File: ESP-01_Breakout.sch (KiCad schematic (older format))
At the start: 136 parts, among them J1 TBL003-254-02GR-2OR, SW1 SW_SPDT, U1 ESP-01v090, U2 R-78E5.0-0.5, U3 R-78E3.3-0.5

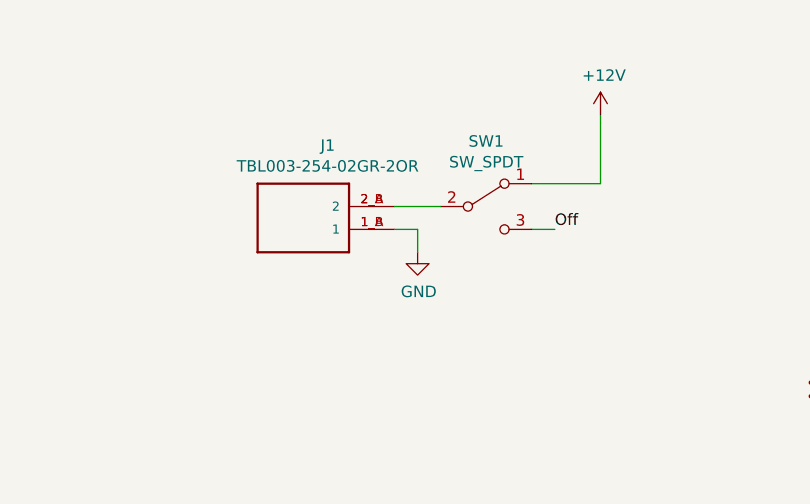
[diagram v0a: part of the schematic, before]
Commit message: Barrel Jack, Smaller Switch
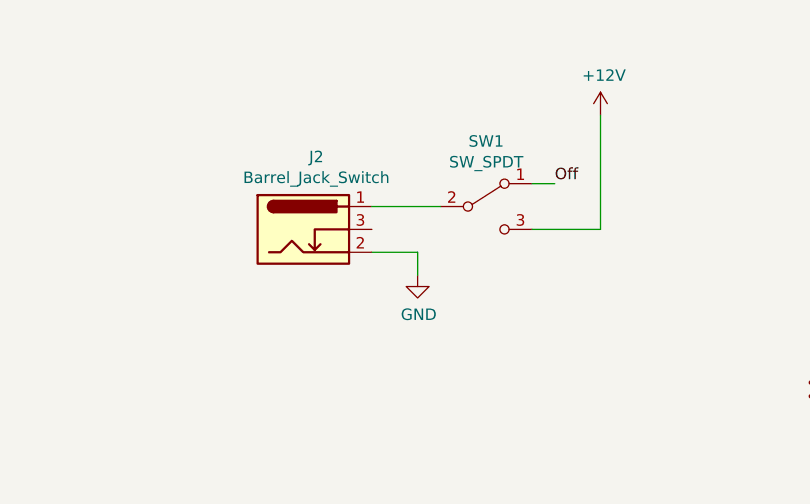
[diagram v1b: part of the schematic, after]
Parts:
- removed J1: TBL003-254-02GR-2OR, TBL003-254-02GR-2OR:CUI_TBL003-254-02GR-2OR, symbol TBL003-254-02GR-2OR:TBL003-254-02GR-2OR
- added J2: Barrel_Jack_Switch, ESP-01_Breakout:BarrelJack_Horizontal, symbol Connector:Barrel_Jack_Switch
- C1: footprint Capacitor_SMD:C_0805_2012Metric_Pad1.15x1.40mm_HandSolder -> Connector_BarrelJack:BarrelJack_Horizontal
- SW1: footprint ESP-01_Breakout:L102011ML04Q -> ESP-01_Breakout:SS312SAH4-R
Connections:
- net +12V: now also SW1.3 (C); no longer SW1.1 (A)
- net GND: now also J2.2
- net Off: now also SW1.1 (A); no longer SW1.3 (C)
- net at SW1.2 (B): now also J2.1
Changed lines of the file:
@@
 F 0 "C1" H 7315 2346 50  0000 L CNN
 F 1 "4.7uF" H 7315 2255 50  0000 L CNN
-F 2 "Capacitor_SMD:C_0805_2012Metric_Pad1.15x1.40mm_HandSolder" H 7238 2150 50  0001 C CNN
+F 2 "Connector_BarrelJack:BarrelJack_Horizontal" H 7238 2150 50  0001 C CNN
 F 3 "~" H 7200 2300 50  0001 C CNN
 F 4 "490-10751-1-ND" H 7200 2300 50  0001 C CNN "DigikeyPN"
@@
 	1100 3600 1200 3600
 $Comp
-L TBL003-254-02GR-2OR:TBL003-254-02GR-2OR J1
-U 1 1 5E644418
-P 4900 1500
-F 0 "J1" H 4793 1233 50  0000 C CNN
-F 1 "TBL003-254-02GR-2OR" H 4793 1324 50  0000 C CNN
-F 2 "TBL003-254-02GR-2OR:CUI_TBL003-254-02GR-2OR" H 4900 1500 50  0001 L BNN
-F 3 "Manufacturer Recommendations" H 4900 1500 50  0001 L BNN
-F 4 "CUI" H 4900 1500 50  0001 L BNN "Field4"
-F 5 "102-6385-ND" H 4900 1500 50  0001 C CNN "DigikeyPN"
-	1    4900 1500
-	-1   0    0    1
-$EndComp
-$Comp
 L power:+12V #PWR0114
 U 1 1 5E64A584
@@
 L power:GND #PWR0115
 U 1 1 5E657F15
-P 5400 1700
-F 0 "#PWR0115" H 5400 1450 50  0001 C CNN
-F 1 "GND" H 5405 1527 50  0000 C CNN
-F 2 "" H 5400 1700 50  0001 C CNN
-F 3 "" H 5400 1700 50  0001 C CNN
-	1    5400 1700
-	1    0    0    -1
-$EndComp
-Wire Wire Line
-	5300 1600 5400 1600
-Wire Wire Line
-	5400 1600 5400 1700
+P 5400 1800
+F 0 "#PWR0115" H 5400 1550 50  0001 C CNN
+F 1 "GND" H 5405 1627 50  0000 C CNN
+F 2 "" H 5400 1800 50  0001 C CNN
+F 3 "" H 5400 1800 50  0001 C CNN
+	1    5400 1800
+	1    0    0    -1
+$EndComp
+Wire Wire Line
+	5200 1700 5400 1700
+Wire Wire Line
+	5400 1700 5400 1800
 $Comp
 L Switch:SW_SPDT SW1
@@
 F 0 "SW1" H 5700 1785 50  0000 C CNN
 F 1 "SW_SPDT" H 5700 1694 50  0000 C CNN
-F 2 "ESP-01_Breakout:L102011ML04Q" H 5700 1500 50  0001 C CNN
+F 2 "ESP-01_Breakout:SS312SAH4-R" H 5700 1500 50  0001 C CNN
 F 3 "~" H 5700 1500 50  0001 C CNN
 F 4 "CKN10652-ND" H 5700 1500 50  0001 C CNN "DigikeyPN"
@@
 $EndComp
 Wire Wire Line
-	5300 1500 5500 1500
-Wire Wire Line
-	5900 1400 6200 1400
-Wire Wire Line
-	6200 1100 6200 1400
+	5200 1500 5500 1500
 Connection ~ 3100 3400
 Connection ~ 3100 3600
@@
 Wire Wire Line
 	2000 4000 1800 4000
-Wire Wire Line
-	6000 1600 5900 1600
-Text Label 6000 1600 0    50   ~ 0
+Text Label 6000 1400 0    50   ~ 0
 Off
+$Comp
+L Connector:Barrel_Jack_Switch J2
+U 1 1 5E50FF0F
+P 4900 1600
+F 0 "J2" H 4957 1917 50  0000 C CNN
+F 1 "Barrel_Jack_Switch" H 4957 1826 50  0000 C CNN
+F 2 "ESP-01_Breakout:BarrelJack_Horizontal" H 4950 1560 50  0001 C CNN
+F 3 "~" H 4950 1560 50  0001 C CNN
+F 4 "2073-DCJ235-05-A-K1-K-ND" H 4900 1600 50  0001 C CNN "DigikeyPN"
+	1    4900 1600
+	1    0    0    -1
+$EndComp
+Wire Wire Line
+	5900 1400 6000 1400
+Wire Wire Line
+	6200 1600 5900 1600
+Wire Wire Line
+	6200 1100 6200 1600
 $EndSCHEMATC

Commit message: BOM, gitignore Update
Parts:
- C1: footprint Connector_BarrelJack:BarrelJack_Horizontal -> Capacitor_SMD:C_0805_2012Metric_Pad1.15x1.40mm_HandSolder
- SW1: DigikeyPN CKN10652-ND -> 360-2924-2-ND
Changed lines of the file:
@@
 F 0 "C1" H 7315 2346 50  0000 L CNN
 F 1 "4.7uF" H 7315 2255 50  0000 L CNN
-F 2 "Connector_BarrelJack:BarrelJack_Horizontal" H 7238 2150 50  0001 C CNN
+F 2 "Capacitor_SMD:C_0805_2012Metric_Pad1.15x1.40mm_HandSolder" H 7238 2150 50  0001 C CNN
 F 3 "~" H 7200 2300 50  0001 C CNN
 F 4 "490-10751-1-ND" H 7200 2300 50  0001 C CNN "DigikeyPN"
@@
 F 2 "ESP-01_Breakout:SS312SAH4-R" H 5700 1500 50  0001 C CNN
 F 3 "~" H 5700 1500 50  0001 C CNN
-F 4 "CKN10652-ND" H 5700 1500 50  0001 C CNN "DigikeyPN"
+F 4 "360-2924-2-ND" H 5700 1500 50  0001 C CNN "DigikeyPN"
 	1    5700 1500
 	1    0    0    -1

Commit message: Update BOM Info
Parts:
- SW1: DigikeyPN 360-2924-2-ND -> 360-2924-1-ND
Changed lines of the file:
@@
 F 2 "ESP-01_Breakout:SS312SAH4-R" H 5700 1500 50  0001 C CNN
 F 3 "~" H 5700 1500 50  0001 C CNN
-F 4 "360-2924-2-ND" H 5700 1500 50  0001 C CNN "DigikeyPN"
+F 4 "360-2924-1-ND" H 5700 1500 50  0001 C CNN "DigikeyPN"
 	1    5700 1500
 	1    0    0    -1

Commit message: Add Inductor 3D Model
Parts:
- L1, L2: footprint RLS-397:IND_RLS-397 -> ESP-01_Breakout:IND_RLS-397
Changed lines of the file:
@@
 F 0 "L2" V 7740 1050 50  0000 C CNN
 F 1 "L" V 7649 1050 50  0000 C CNN
-F 2 "RLS-397:IND_RLS-397" H 7550 1050 50  0001 C CNN
+F 2 "ESP-01_Breakout:IND_RLS-397" H 7550 1050 50  0001 C CNN
 F 3 "~" H 7550 1050 50  0001 C CNN
 F 4 "945-30004967-ND" H 7550 1050 50  0001 C CNN "DigikeyPN"
@@
 F 0 "L1" V 7690 2100 50  0000 C CNN
 F 1 "L" V 7599 2100 50  0000 C CNN
-F 2 "RLS-397:IND_RLS-397" H 7500 2100 50  0001 C CNN
+F 2 "ESP-01_Breakout:IND_RLS-397" H 7500 2100 50  0001 C CNN
 F 3 "~" H 7500 2100 50  0001 C CNN
 F 4 "945-30004967-ND" H 7500 2100 50  0001 C CNN "DigikeyPN"

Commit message: Updated Footprints, Added 5v Solder Jumper
Slight tweak to silkscreen tezt
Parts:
- added JP1: SolderJumper_2_Open, Jumper:SolderJumper-2_P1.3mm_Open_TrianglePad1.0x1.5mm, symbol Jumper:SolderJumper_2_Open
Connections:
- net +12V: now also JP1.2 (B); no longer C2.1, L2.1
- new net: C2.1, JP1.1 (A), L2.1
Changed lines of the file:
@@
 L power:+12V #PWR0106
 U 1 1 5E57F846
-P 7250 900
-F 0 "#PWR0106" H 7250 750 50  0001 C CNN
-F 1 "+12V" H 7265 1073 50  0000 C CNN
-F 2 "" H 7250 900 50  0001 C CNN
-F 3 "" H 7250 900 50  0001 C CNN
-	1    7250 900
+P 7250 650
+F 0 "#PWR0106" H 7250 500 50  0001 C CNN
+F 1 "+12V" H 7265 823 50  0000 C CNN
+F 2 "" H 7250 650 50  0001 C CNN
+F 3 "" H 7250 650 50  0001 C CNN
+	1    7250 650
 	1    0    0    -1
 $EndComp
@@
 Connection ~ 7850 1050
 Wire Wire Line
-	7250 900  7250 1050
-Connection ~ 7250 1050
-Wire Wire Line
 	7250 1500 7250 1400
 Wire Wire Line
@@
 Wire Wire Line
 	6200 1100 6200 1600
+$Comp
+L Jumper:SolderJumper_2_Open JP1
+U 1 1 5E5B755B
+P 7250 850
+F 0 "JP1" H 7250 1055 50  0000 C CNN
+F 1 "SolderJumper_2_Open" H 7250 964 50  0000 C CNN
+F 2 "Jumper:SolderJumper-2_P1.3mm_Open_TrianglePad1.0x1.5mm" H 7250 850 50  0001 C CNN
+F 3 "~" H 7250 850 50  0001 C CNN
+	1    7250 850
+	0    -1   -1   0
+$EndComp
+Wire Wire Line
+	7250 650  7250 700
+Wire Wire Line
+	7250 1000 7250 1050
+Connection ~ 7250 1050
 $EndSCHEMATC
